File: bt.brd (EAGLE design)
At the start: 24.4 x 17.8 mm, 16 parts, among them Q1 MOSFET-NCHANNELSMD, Q2 MOSFET-NCHANNELSMD

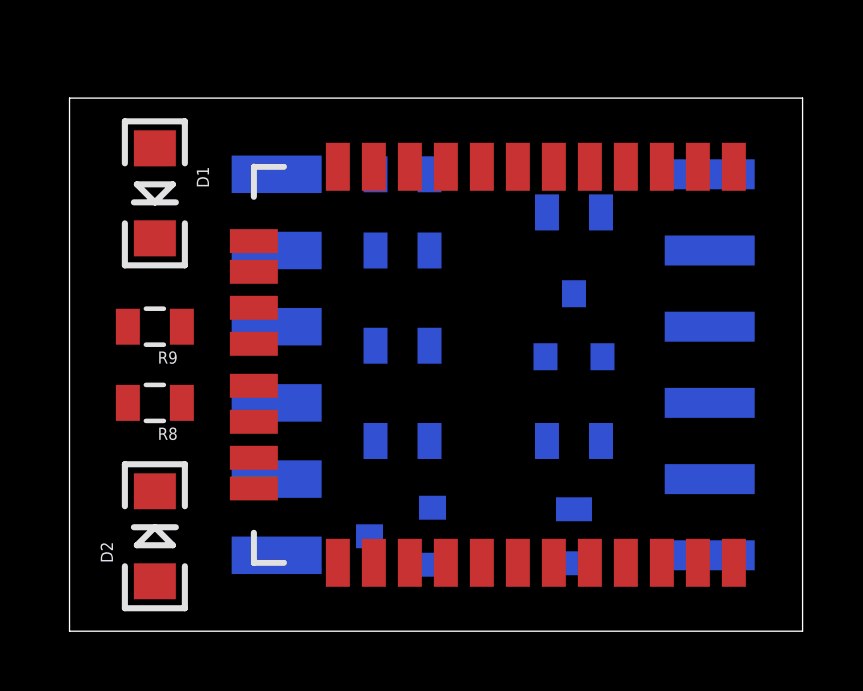
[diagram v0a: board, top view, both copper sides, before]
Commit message: Got a good handle on the bt module so went ahead and ordered one
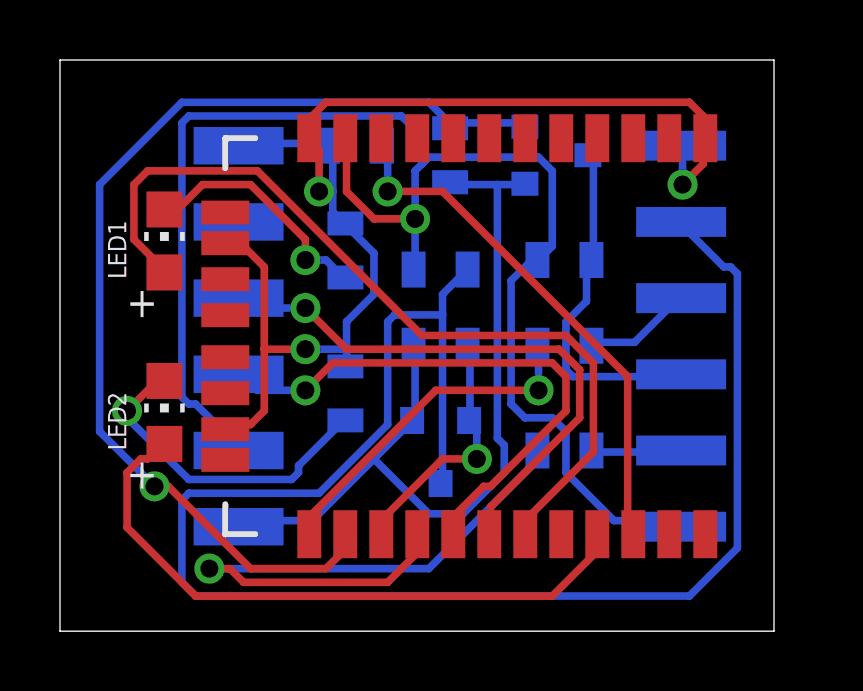
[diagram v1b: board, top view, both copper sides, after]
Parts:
- removed D1, D2: (no value), SparkFun-LED:LED-1206
- added LED1, LED2: (no value), adafruit:CHIP-LED0805
- moved R2 10.7 mm to (16.8, 6.03), turned to 180 degrees
- moved R3 10.4 mm to (13.0, 15.9), turned to 270 degrees
- moved R5 7.75 mm to (12.7, 9.53), turned to 0 degrees
- moved R9 6.84 mm to (9.53, 12.7), flipped to the bottom, turned to 270 degrees
- moved R8 6.36 mm to (9.53, 7.94), flipped to the bottom, turned to 270 degrees
- moved R6 5.85 mm to (12.7, 12.1)
- moved Q1 5.75 mm to (16.5, 15.9), turned to 90 degrees
- moved R1 5.40 mm to (16.8, 9.53), turned to 180 degrees
- moved R7 3.84 mm to (9.84, 16.2)
- moved Q2 3.13 mm to (12.7, 6.03), turned to 180 degrees
- moved R4 1.62 mm to (16.8, 12.4)
- moved USB 1.59 mm to (2.54, 9.84)
- moved RN-42HID 1.35 mm to (14.9, 9.84)
- moved UART 1.35 mm to (25.7, 9.84)
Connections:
- net N$1: now also LED2.C; no longer D2.C
- net N$10: now also LED2.A; no longer D2.A
- net N$3: now also LED1.C; no longer D1.C
- net N$8: now also LED1.A; no longer D1.A
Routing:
- net UART_RTS_5V: track 0.00 -> 54.6 mm
- net VCC: track 0.00 -> 50.5 mm, vias 0 -> 1
- net GND: track 0.00 -> 42.6 mm, vias 0 -> 3
- net UART_TX: track 0.00 -> 35.1 mm, vias 0 -> 1
- net N$8: track 0.00 -> 28.1 mm
- net 3.3V: track 0.00 -> 27.7 mm
- net N$10: track 0.00 -> 21.3 mm
- net UART_CTS: track 0.00 -> 21.0 mm, vias 0 -> 1
- net USB_D+: track 0.00 -> 19.1 mm, vias 0 -> 1
- net USB_D-: track 0.00 -> 18.6 mm, vias 0 -> 1
- net N$9: track 0.00 -> 17.5 mm, vias 0 -> 1
- net UART_TX_5V: track 0.00 -> 11.7 mm
- net UART_RX: track 0.00 -> 11.4 mm, vias 0 -> 1
- net N$1: track 0.00 -> 11.1 mm, vias 0 -> 1
- net UART_RTS: track 0.00 -> 8.39 mm, vias 0 -> 1
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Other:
- board size 24.4 x 17.8 mm -> 23.8 x 19 mm
